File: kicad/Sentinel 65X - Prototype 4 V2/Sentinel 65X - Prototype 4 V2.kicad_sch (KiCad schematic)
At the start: 29 parts, among them J1 USB_C_Receptacle_USB2.0_14P, U1 FT230XS, U2 NCP1117-3.3_SOT223, X1 ECS-327MVATX-5-CN-TR, X2 ASF1-3.686MHZ-N-K-S, X3 ECS-3963-250-BN-TR, X4 ECS-5032MV-80-CN-TR

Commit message: Updated prototype 4 V2 schematic
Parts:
- removed C1, C2: 47pF, Capacitor_SMD:C_0402_1005Metric, symbol Device:C
- removed C10, C3, C4, C5, C6, C7, C9: 100nF, Capacitor_SMD:C_0402_1005Metric, symbol Device:C
- removed C11, C8: 10µF, Capacitor_SMD:CP_Elec_4x5.4, symbol Device:C_Polarized
- removed J1: USB_C_Receptacle_USB2.0_14P, Connector_USB:USB_C_Receptacle_GCT_USB4085, symbol Connector:USB_C_Receptacle_USB2.0_14P
- removed R1, R2: 270Ω, Resistor_SMD:R_0402_1005Metric, symbol Device:R
- removed R10, R11, R5, R6, R7, R8, R9: 3.3KΩ, Resistor_SMD:R_0402_1005Metric, symbol Device:R
- removed R3, R4: 5.1KΩ, Resistor_SMD:R_0402_1005Metric, symbol Device:R
- removed U1: FT230XS, Package_SO:SSOP-16_3.9x4.9mm_P0.635mm, symbol Interface_USB:FT230XS
- removed U2: NCP1117-3.3_SOT223, Package_TO_SOT_SMD:SOT-223-3_TabPin2, symbol Regulator_Linear:NCP1117-3.3_SOT223
- removed X1: ECS-327MVATX-5-CN-TR, Oscillator:Oscillator_SMD_EuroQuartz_XO53-4Pin_5.0x3.2mm_HandSoldering, symbol Oscillator:XO53
- removed X2: ASF1-3.686MHZ-N-K-S, Oscillator:Oscillator_SMD_EuroQuartz_XO53-4Pin_5.0x3.2mm_HandSoldering, symbol Oscillator:XO53
- removed X3: ECS-3963-250-BN-TR, Oscillator:Oscillator_SMD_EuroQuartz_XO53-4Pin_5.0x3.2mm_HandSoldering, symbol Oscillator:XO53
- removed X4: ECS-5032MV-80-CN-TR, Oscillator:Oscillator_SMD_EuroQuartz_XO53-4Pin_5.0x3.2mm_HandSoldering, symbol Oscillator:XO53
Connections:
- no-connect marks 4 -> 0
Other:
- added sheet AV Port (AV Port.kicad_sch)
- added sheet Cartridge Port (Cartridge Port.kicad_sch)
- added sheet Expansion Ports (Expansion Ports.kicad_sch)
- added sheet Glue Logic (Glue Logic.kicad_sch)
- added sheet IO Port (IO Port.kicad_sch)
- added sheet Power Supply (Power Supply.kicad_sch)
- added sheet System Memory (System Memory.kicad_sch)
- added sheet VERA (VERA.kicad_sch)
- added sheet W65C265S CPU (W65C265S CPU.kicad_sch)
- note added: "Unmarked capacitors are CL05A_{10}6MQ5NUNC 10uF 6.3V 0402"

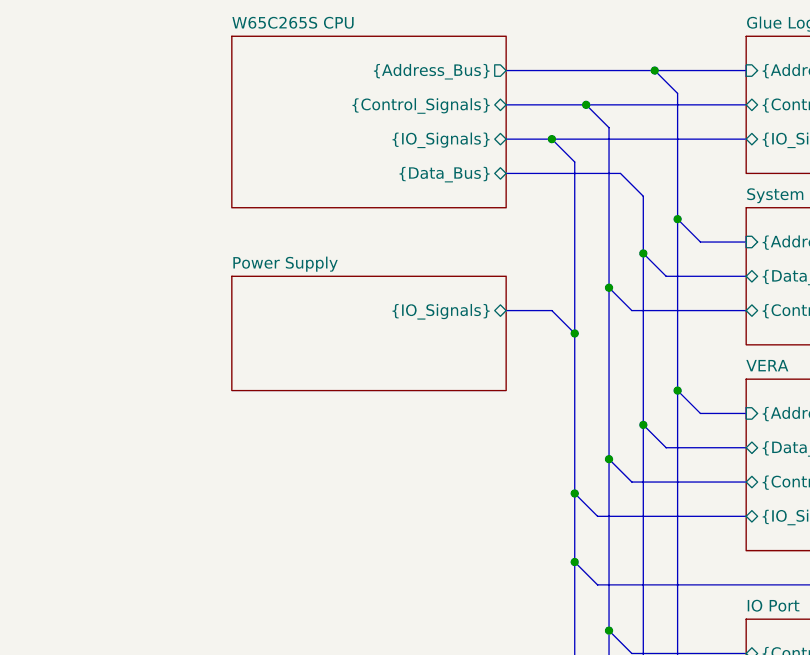
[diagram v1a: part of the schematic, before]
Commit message: Updated prototype 4V2 schematic
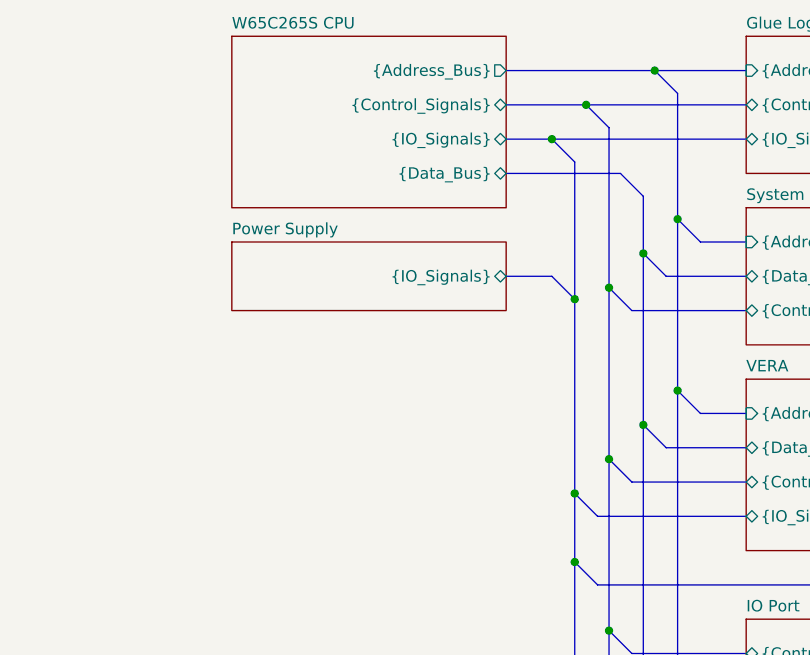
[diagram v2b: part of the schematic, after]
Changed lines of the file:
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@@
 		(members "SNES_DATA_{[0..9]}" "SNES_LATCH" "SNES_CLK" "LED_{[0..9]}" "MULTI_BTN"
 			"SDA" "SCL" "MISO" "MOSI" "SCK" "~{SD_SS}" "TXD" "RXD" "~{RTS}" "~{CTS}"
-			"~{FPGA_SS}" "~{FLASH_SS}" "~{SD_WP}" "~{SD_CD}"
+			"~{FPGA_SS}" "~{FLASH_SS}" "~{SD_WP}" "~{SD_CD}" "~{CART}"
 		)
 	)
@@
 	)
 	(junction
-		(at 96.52 69.85)
+		(at 96.52 106.68)
 		(diameter 0)
 		(color 255 143 55 1)
 	)
 	(junction
-		(at 96.52 106.68)
+		(at 100.33 64.77)
+		(diameter 0)
+		(color 0 0 0 0)
+	)
+	(junction
+		(at 104.14 121.92)
+		(diameter 0)
+		(color 61 222 255 1)
+	)
+	(junction
+		(at 105.41 40.64)
+		(diameter 0)
+		(color 59 191 91 1)
+	)
+	(junction
+		(at 104.14 60.96)
+		(diameter 0)
+		(color 61 222 255 1)
+	)
+	(junction
+		(at 107.95 118.11)
+		(diameter 0)
+		(color 59 191 91 1)
+	)
+	(junction
+		(at 96.52 95.25)
 		(diameter 0)
 		(color 255 143 55 1)
 	)
 	(junction
-		(at 100.33 64.77)
+		(at 96.52 66.04)
 		(diameter 0)
 		(color 0 0 0 0)
 	)
 	(junction
-		(at 104.14 121.92)
-		(diameter 0)
-		(color 61 222 255 1)
-	)
-	(junction
-		(at 105.41 40.64)
-		(diameter 0)
-		(color 59 191 91 1)
-	)
-	(junction
-		(at 104.14 60.96)
-		(diameter 0)
-		(color 61 222 255 1)
-	)
-	(junction
-		(at 107.95 118.11)
-		(diameter 0)
-		(color 59 191 91 1)
-	)
-	(junction
-		(at 96.52 95.25)
+		(at 100.33 83.82)
+		(diameter 0)
+		(color 0 0 0 0)
+	)
+	(junction
+		(at 100.33 102.87)
+		(diameter 0)
+		(color 0 0 0 0)
+	)
+	(junction
+		(at 100.33 125.73)
+		(diameter 0)
+		(color 0 0 0 0)
+	)
+	(junction
+		(at 96.52 87.63)
 		(diameter 0)
 		(color 255 143 55 1)
 	)
-	(junction
-		(at 100.33 83.82)
-		(diameter 0)
-		(color 0 0 0 0)
-	)
-	(junction
-		(at 100.33 102.87)
-		(diameter 0)
-		(color 0 0 0 0)
-	)
-	(junction
-		(at 100.33 125.73)
-		(diameter 0)
-		(color 0 0 0 0)
-	)
-	(junction
-		(at 96.52 87.63)
-		(diameter 0)
-		(color 255 143 55 1)
-	)
 	(bus
 		(pts
@@
 	(bus
 		(pts
-			(xy 88.9 67.31) (xy 93.98 67.31)
+			(xy 88.9 63.5) (xy 93.98 63.5)
 		)
 		(stroke
@@
 	(bus
 		(pts
-			(xy 96.52 69.85) (xy 96.52 87.63)
+			(xy 96.52 66.04) (xy 96.52 87.63)
 		)
 		(stroke
@@
 	(bus
 		(pts
-			(xy 96.52 50.8) (xy 96.52 69.85)
+			(xy 96.52 50.8) (xy 96.52 66.04)
 		)
 		(stroke
@@
 	(bus
 		(pts
-			(xy 96.52 69.85) (xy 93.98 67.31)
+			(xy 96.52 66.04) (xy 93.98 63.5)
 		)
 		(stroke
@@
 	)
 	(sheet
-		(at 58.42 63.5)
-		(size 30.48 12.7)
+		(at 58.42 59.69)
+		(size 30.48 7.62)
 		(fields_autoplaced yes)
 		(stroke
@@
 		)
 		(property "Sheetname" "Power Supply"
-			(at 58.42 62.7884 0)
+			(at 58.42 58.9784 0)
 			(effects
 				(font
@@
 		)
 		(property "Sheetfile" "Power Supply.kicad_sch"
-			(at 58.42 76.7846 0)
+			(at 58.42 67.8946 0)
 			(effects
 				(font
@@
 		)
 		(pin "{IO_Signals}" bidirectional
-			(at 88.9 67.31 0)
-			(effects
-				(font
+			(at 88.9 63.5 0)
+			(effects
+				(font
